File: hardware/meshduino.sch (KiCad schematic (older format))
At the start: 9 parts, among them P1 mPCIe, P2 USB, U1 SM200, U2 FT232RL

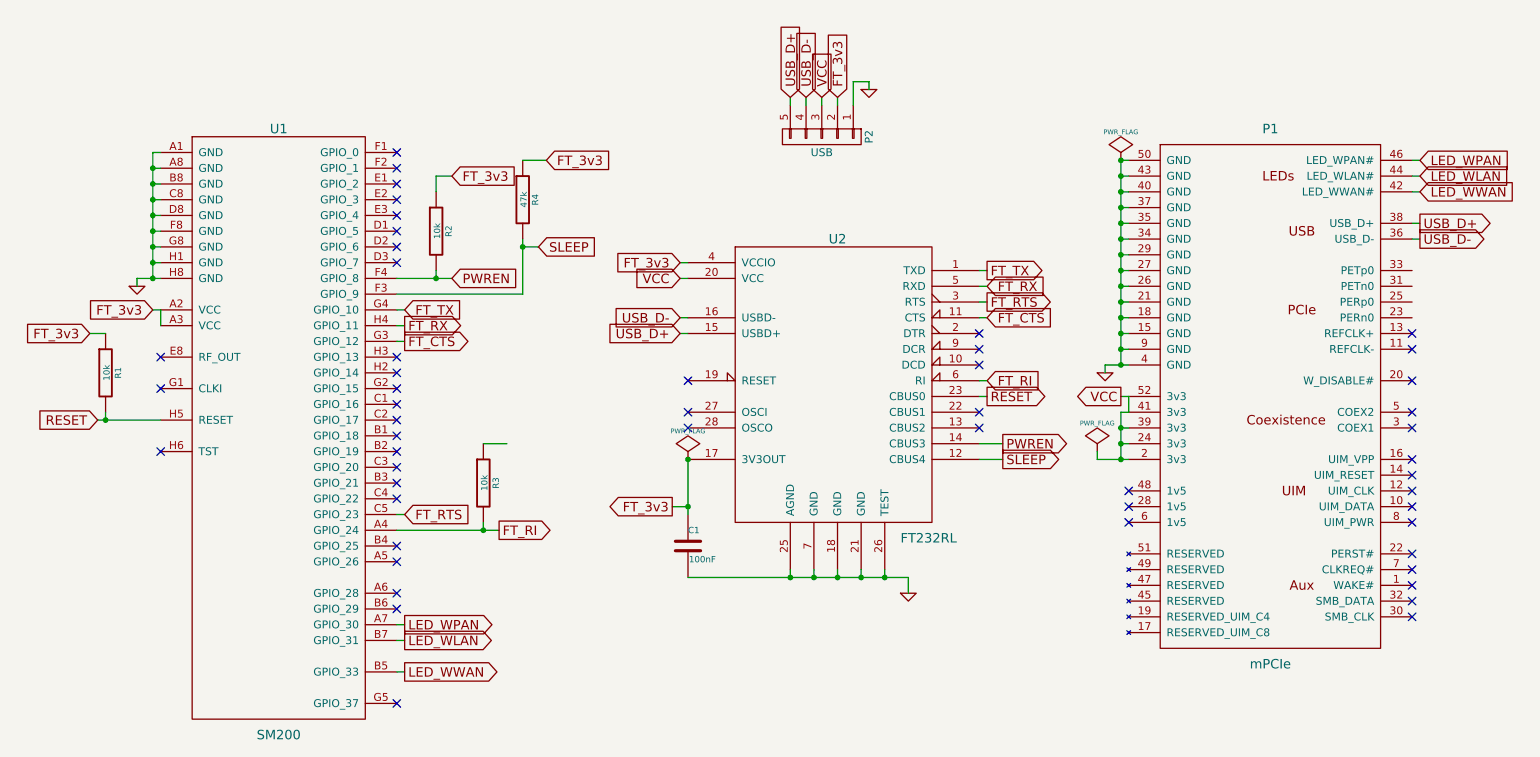
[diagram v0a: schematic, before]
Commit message: Replace pcie connector with USB connector.
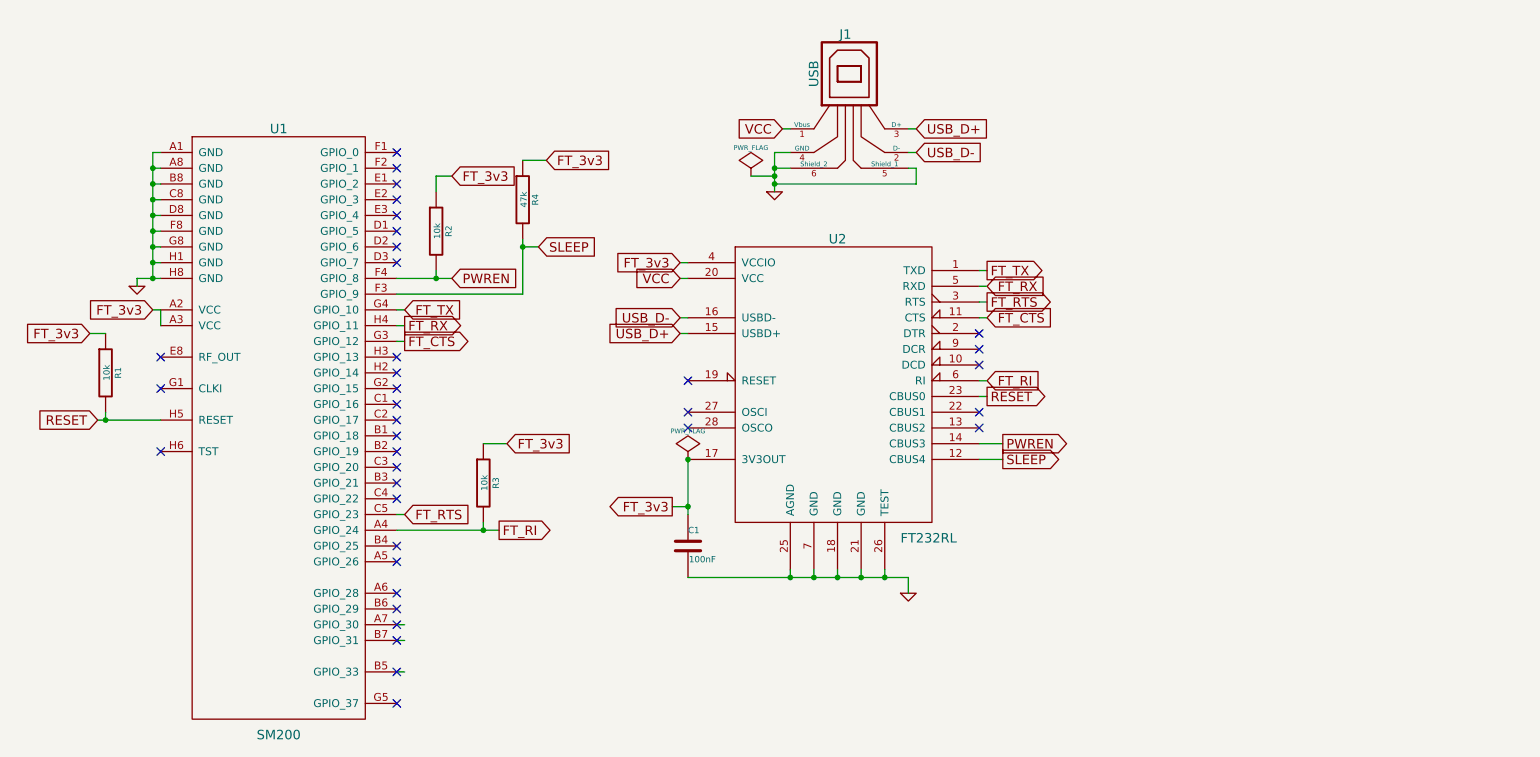
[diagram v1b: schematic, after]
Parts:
- removed P1: mPCIe, _CrumpPrints:MPCIe_full_card, symbol mPCIe
- removed P2: USB, Pin_Headers:Pin_Header_Straight_1x05, symbol CONN_01X05
- added J1: USB, symbol USB
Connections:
- net labels removed: LED_WLAN, LED_WPAN, LED_WWAN
- wire segments 91 -> 65
- no-connect marks 52 -> 37
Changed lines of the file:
@@
-$EndComp
-$Comp
-L mPCIe P1
-U 1 1 55C19570
-P 9350 3500
-F 0 "P1" H 9350 4900 60  0000 C CNN
-F 1 "mPCIe" H 9350 1500 60  0000 C CNN
-F 2 "_CrumpPrints:MPCIe_full_card" H 9350 3500 60  0001 C CNN
-F 3 "" H 9350 3500 60  0000 C CNN
-	1    9350 3500
-	1    0    0    -1
 $EndComp
 $Comp
@@
 	1    0    0    -1
 $EndComp
-Text GLabel 10300 2700 2    60   Output ~ 0
-USB_D+
-Text GLabel 10300 2800 2    60   Output ~ 0
-USB_D-
 Text GLabel 5600 3400 0    60   Input ~ 0
 USB_D+
@@
 USB_D-
 Text GLabel 5600 3050 0    60   Input ~ 0
-VCC
-Text GLabel 8400 3800 0    60   Output ~ 0
 VCC
 Text GLabel 2250 3250 0    60   Input ~ 0
@@
 Text GLabel 5600 2950 0    60   Input ~ 0
 FT_3v3
-Text GLabel 10300 2300 2    60   Input ~ 0
-LED_WPAN
-Text GLabel 10300 2400 2    60   Input ~ 0
-LED_WLAN
-Text GLabel 10300 2500 2    60   Input ~ 0
-LED_WWAN
-Text GLabel 3850 5550 2    60   Output ~ 0
-LED_WWAN
-Text GLabel 3850 5350 2    60   Output ~ 0
-LED_WLAN
-Text GLabel 3850 5250 2    60   Output ~ 0
-LED_WPAN
 $Comp
 L GND #PWR02
@@
 	1    0    0    -1
 $EndComp
-$Comp
-L GND #PWR03
-U 1 1 55FF26A9
-P 8300 3650
-F 0 "#PWR03" H 8300 3650 30  0001 C CNN
-F 1 "GND" H 8300 3580 30  0001 C CNN
-F 2 "" H 8300 3650 60  0000 C CNN
-F 3 "" H 8300 3650 60  0000 C CNN
-	1    8300 3650
-	1    0    0    -1
-$EndComp
 Wire Wire Line
 	5600 3300 5650 3300
 Wire Wire Line
 	5600 3400 5650 3400
-Wire Wire Line
-	10250 2700 10300 2700
-Wire Wire Line
-	10250 2800 10300 2800
-Wire Wire Line
-	8400 3800 8450 3800
 Wire Wire Line
 	5600 3050 5650 3050
@@
 	4600 3150 3800 3150
 Wire Wire Line
-	6450 4900 6450 4950
+	6450 4950 6450 4900
 Wire Wire Line
 	5650 4950 7050 4950
@@
 	4050 2400 4150 2400
 Wire Wire Line
-	10250 2500 10300 2500
-Wire Wire Line
-	10250 2400 10300 2400
-Wire Wire Line
-	10250 2300 10300 2300
-Wire Wire Line
 	3800 5250 3850 5250
 Wire Wire Line
@@
 	3800 5550 3850 5550
 Wire Wire Line
-	8450 2300 8400 2300
-Wire Wire Line
-	8400 2300 8400 3600
-Wire Wire Line
-	8400 2400 8450 2400
-Wire Wire Line
-	8400 2500 8450 2500
-Connection ~ 8400 2400
-Wire Wire Line
-	8400 2600 8450 2600
-Connection ~ 8400 2500
-Wire Wire Line
-	8400 2700 8450 2700
-Connection ~ 8400 2600
-Wire Wire Line
-	8400 2800 8450 2800
-Connection ~ 8400 2700
-Wire Wire Line
-	8400 2900 8450 2900
-Connection ~ 8400 2800
-Wire Wire Line
-	8400 3000 8450 3000
-Connection ~ 8400 2900
-Wire Wire Line
-	8400 3100 8450 3100
-Connection ~ 8400 3000
-Wire Wire Line
-	8400 3200 8450 3200
-Connection ~ 8400 3100
-Wire Wire Line
-	8400 3300 8450 3300
-Connection ~ 8400 3200
-Wire Wire Line
-	8400 3400 8450 3400
-Connection ~ 8400 3300
-Wire Wire Line
-	8400 3500 8450 3500
-Connection ~ 8400 3400
-Wire Wire Line
-	8300 3600 8450 3600
-Connection ~ 8400 3500
-Wire Wire Line
-	8450 3800 8450 3900
-Wire Wire Line
-	8400 3900 8400 4200
-Wire Wire Line
-	8400 4000 8450 4000
-Wire Wire Line
-	8450 3900 8400 3900
-Wire Wire Line
-	8400 4100 8450 4100
-Connection ~ 8400 4000
-Wire Wire Line
-	8250 4200 8450 4200
-Connection ~ 8400 4100
-Wire Wire Line
-	8300 3600 8300 3650
-Connection ~ 8400 3600
-Wire Wire Line
-	2300 3050 2150 3050
+	2150 3050 2300 3050
 Wire Wire Line
 	2150 3050 2150 3100
@@
 	2250 2250 2300 2250
 Connection ~ 2250 2350
-NoConn ~ 10250 3400
-NoConn ~ 10250 3500
-NoConn ~ 10250 3700
-NoConn ~ 10250 3900
-NoConn ~ 10250 4000
-NoConn ~ 10250 4200
-NoConn ~ 10250 4300
-NoConn ~ 10250 4400
-NoConn ~ 10250 4500
-NoConn ~ 10250 4600
-NoConn ~ 10250 4800
-NoConn ~ 10250 4900
-NoConn ~ 10250 5000
-NoConn ~ 10250 5100
-NoConn ~ 10250 5200
-NoConn ~ 8450 4600
-NoConn ~ 8450 4500
-NoConn ~ 8450 4400
 NoConn ~ 7500 3400
 NoConn ~ 7500 3500
@@
 NoConn ~ 3800 5150
 $Comp
-L PWR_FLAG #FLG04
-U 1 1 55FF3712
-P 8400 2300
-F 0 "#FLG04" H 8400 2395 30  0001 C CNN
-F 1 "PWR_FLAG" H 8400 2480 30  0000 C CNN
-F 2 "" H 8400 2300 60  0000 C CNN
-F 3 "" H 8400 2300 60  0000 C CNN
-	1    8400 2300
-	1    0    0    -1
-$EndComp
-Connection ~ 8400 2300
-$Comp
-L PWR_FLAG #FLG05
-U 1 1 55FF3839
-P 8250 4150
-F 0 "#FLG05" H 8250 4245 30  0001 C CNN
-F 1 "PWR_FLAG" H 8250 4330 30  0000 C CNN
-F 2 "" H 8250 4150 60  0000 C CNN
-F 3 "" H 8250 4150 60  0000 C CNN
-	1    8250 4150
-	1    0    0    -1
-$EndComp
-Wire Wire Line
-	8250 4150 8250 4200
-Connection ~ 8400 4200
-$Comp
-L PWR_FLAG #FLG06
+L PWR_FLAG #FLG03
 U 1 1 55FF4264
 P 5650 4200
-F 0 "#FLG06" H 5650 4295 30  0001 C CNN
+F 0 "#FLG03" H 5650 4295 30  0001 C CNN
 F 1 "PWR_FLAG" H 5650 4380 30  0000 C CNN
 F 2 "" H 5650 4200 60  0000 C CNN
@@
 Connection ~ 5650 4200
 $Comp
-L CONN_01X05 P2
-U 1 1 55FF44AF
-P 6500 2150
-F 0 "P2" H 6500 2450 50  0000 C CNN
-F 1 "USB" V 6600 2150 50  0000 C CNN
-F 2 "Pin_Headers:Pin_Header_Straight_1x05" H 6500 2150 60  0001 C CNN
-F 3 "" H 6500 2150 60  0000 C CNN
-	1    6500 2150
-	0    1    1    0
-$EndComp
-$Comp
-L GND #PWR07
+L GND #PWR04
 U 1 1 55FF454C
-P 6800 1850
-F 0 "#PWR07" H 6800 1850 30  0001 C CNN
-F 1 "GND" H 6800 1780 30  0001 C CNN
-F 2 "" H 6800 1850 60  0000 C CNN
-F 3 "" H 6800 1850 60  0000 C CNN
-	1    6800 1850
-	1    0    0    -1
-$EndComp
-Text GLabel 6500 1900 1    60   Input ~ 0
+P 6200 2500
+F 0 "#PWR04" H 6200 2500 30  0001 C CNN
+F 1 "GND" H 6200 2430 30  0001 C CNN
+F 2 "" H 6200 2500 60  0000 C CNN
+F 3 "" H 6200 2500 60  0000 C CNN
+	1    6200 2500
+	1    0    0    -1
+$EndComp
+Text GLabel 6250 2100 0    60   Input ~ 0
 VCC
-Text GLabel 6600 1900 1    60   Input ~ 0
-FT_3v3
-Text GLabel 6400 1900 1    60   Input ~ 0
+Text GLabel 7100 2250 2    60   Input ~ 0
 USB_D-
-Text GLabel 6300 1900 1    60   Input ~ 0
+Text GLabel 7100 2100 2    60   Input ~ 0
 USB_D+
-Wire Wire Line
-	6800 1850 6800 1800
-Wire Wire Line
-	6800 1800 6700 1800
-Wire Wire Line
-	6700 1800 6700 1950
-Wire Wire Line
-	6600 1900 6600 1950
-Wire Wire Line
-	6500 1950 6500 1900
-Wire Wire Line
-	6400 1900 6400 1950
-Wire Wire Line
-	6300 1950 6300 1900
 NoConn ~ 5650 3900
 NoConn ~ 5650 4000
+$Comp
+L USB J1
+U 1 1 56207A99
+P 6700 1900
+F 0 "J1" H 6650 2300 60  0000 C CNN
+F 1 "USB" V 6450 2050 60  0000 C CNN
+F 2 "" H 6700 1900 60  0000 C CNN
+F 3 "" H 6700 1900 60  0000 C CNN
+	1    6700 1900
+	1    0    0    -1
+$EndComp
+Wire Wire Line
+	6250 2100 6300 2100
+Wire Wire Line
+	6300 2250 6200 2250
+Wire Wire Line
+	6200 2250 6200 2500
+Wire Wire Line
+	6300 2350 6200 2350
+Connection ~ 6200 2350
+Wire Wire Line
+	7050 2100 7100 2100
+Wire Wire Line
+	7050 2250 7100 2250
+Wire Wire Line
+	7050 2350 7100 2350
+Wire Wire Line
+	7100 2350 7100 2450
+Wire Wire Line
+	7100 2450 6200 2450
+Connection ~ 6200 2450
+NoConn ~ 3800 5250
+NoConn ~ 3800 5350
+NoConn ~ 3800 5550
+$Comp
+L PWR_FLAG #FLG05
+U 1 1 56208562
+P 6050 2400
+F 0 "#FLG05" H 6050 2495 30  0001 C CNN
+F 1 "PWR_FLAG" H 6050 2580 30  0000 C CNN
+F 2 "" H 6050 2400 60  0000 C CNN
+F 3 "" H 6050 2400 60  0000 C CNN
+	1    6050 2400
+	1    0    0    -1
+$EndComp
+Wire Wire Line
+	6050 2400 6200 2400
+Connection ~ 6200 2400
+Text GLabel 4500 4100 2    60   Input ~ 0
+FT_3v3
 $EndSCHEMATC

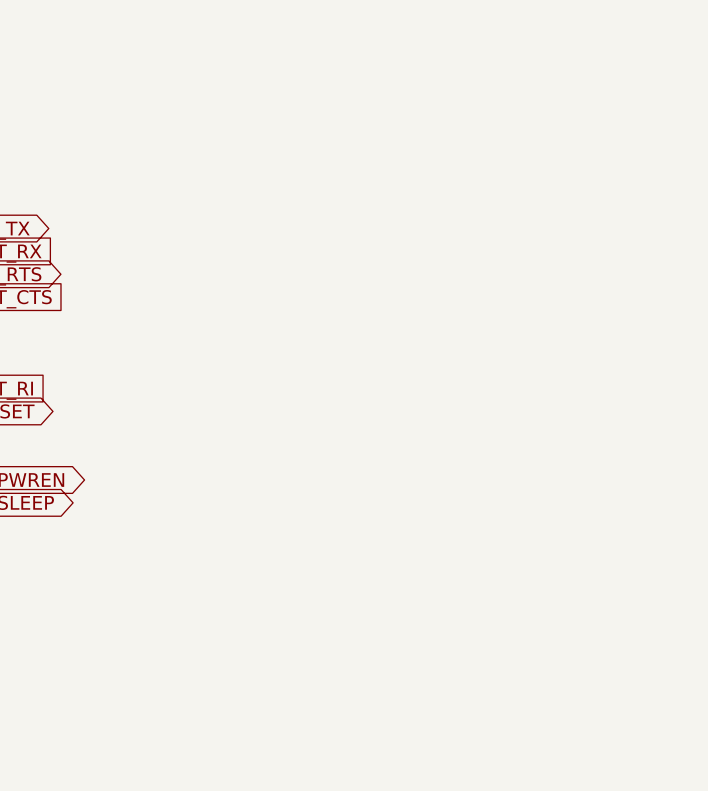
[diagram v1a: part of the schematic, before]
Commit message: Add pin headers to schematic.
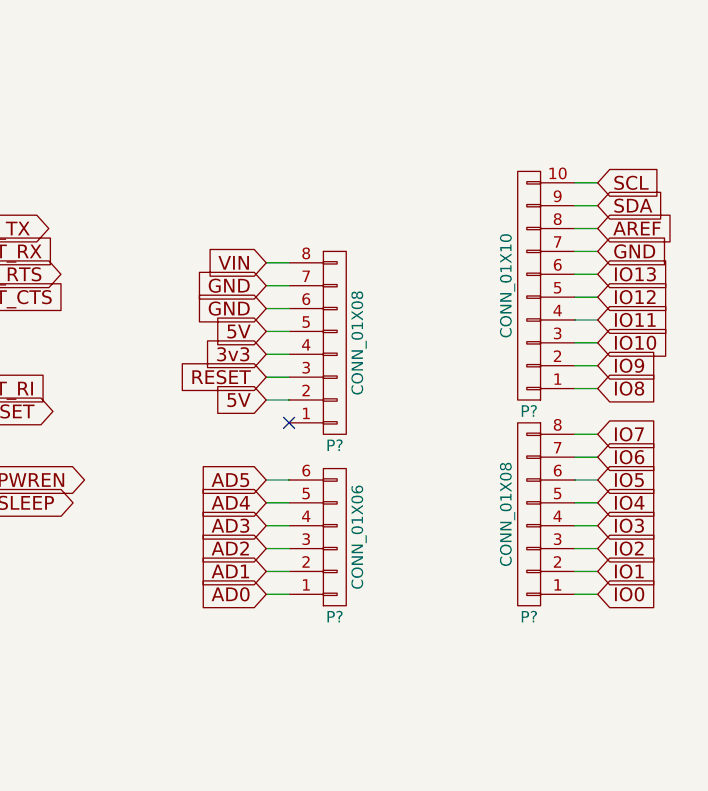
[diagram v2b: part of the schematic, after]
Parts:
- added P?: CONN_01X06, symbol CONN_01X06
- added P? (x2): CONN_01X08, symbol CONN_01X08
- added P?: CONN_01X10, symbol CONN_01X10
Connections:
- net labels added: 3v3, 5V, AD0, AD1, AD2, AD3, AD4, AD5, AREF, IO0, IO1, IO10, IO11, IO12, IO13, IO2, IO3, IO4, IO5, IO6, IO7, IO8, IO9, SCL, SDA, VIN
- wire segments 65 -> 96
- no-connect marks 37 -> 38
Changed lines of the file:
@@
 Text GLabel 4500 4100 2    60   Input ~ 0
 FT_3v3
+$Comp
+L CONN_01X06 P?
+U 1 1 56208AD2
+P 9150 4350
+F 0 "P?" H 9150 4700 50  0000 C CNN
+F 1 "CONN_01X06" V 9250 4350 50  0000 C CNN
+F 2 "" H 9150 4350 60  0000 C CNN
+F 3 "" H 9150 4350 60  0000 C CNN
+	1    9150 4350
+	1    0    0    1
+$EndComp
+$Comp
+L CONN_01X08 P?
+U 1 1 56208B19
+P 9150 3500
+F 0 "P?" H 9150 3950 50  0000 C CNN
+F 1 "CONN_01X08" V 9250 3500 50  0000 C CNN
+F 2 "" H 9150 3500 60  0000 C CNN
+F 3 "" H 9150 3500 60  0000 C CNN
+	1    9150 3500
+	1    0    0    1
+$EndComp
+$Comp
+L CONN_01X08 P?
+U 1 1 56208BBE
+P 10000 4250
+F 0 "P?" H 10000 4700 50  0000 C CNN
+F 1 "CONN_01X08" V 10100 4250 50  0000 C CNN
+F 2 "" H 10000 4250 60  0000 C CNN
+F 3 "" H 10000 4250 60  0000 C CNN
+	1    10000 4250
+	-1   0    0    1
+$EndComp
+$Comp
+L CONN_01X10 P?
+U 1 1 56208C0F
+P 10000 3250
+F 0 "P?" H 10000 3800 50  0000 C CNN
+F 1 "CONN_01X10" V 10100 3250 50  0000 C CNN
+F 2 "" H 10000 3250 60  0000 C CNN
+F 3 "" H 10000 3250 60  0000 C CNN
+	1    10000 3250
+	-1   0    0    1
+$EndComp
+Text GLabel 10300 4600 2    60   Input ~ 0
+IO0
+Text GLabel 10300 4500 2    60   Input ~ 0
+IO1
+Text GLabel 10300 4400 2    60   Input ~ 0
+IO2
+Text GLabel 10300 4300 2    60   Input ~ 0
+IO3
+Text GLabel 10300 4200 2    60   Input ~ 0
+IO4
+Text GLabel 10300 4100 2    60   Input ~ 0
+IO5
+Text GLabel 10300 4000 2    60   Input ~ 0
+IO6
+Text GLabel 10300 3900 2    60   Input ~ 0
+IO7
+Text GLabel 10300 3700 2    60   Input ~ 0
+IO8
+Text GLabel 10300 3600 2    60   Input ~ 0
+IO9
+Text GLabel 10300 3500 2    60   Input ~ 0
+IO10
+Text GLabel 10300 3400 2    60   Input ~ 0
+IO11
+Text GLabel 10300 3300 2    60   Input ~ 0
+IO12
+Text GLabel 10300 3200 2    60   Input ~ 0
+IO13
+Text GLabel 10300 3100 2    60   Input ~ 0
+GND
+Text GLabel 10300 3000 2    60   Input ~ 0
+AREF
+Text GLabel 10300 2900 2    60   Input ~ 0
+SDA
+Text GLabel 10300 2800 2    60   Input ~ 0
+SCL
+Text GLabel 8850 4600 0    60   Input ~ 0
+AD0
+Text GLabel 8850 4500 0    60   Input ~ 0
+AD1
+Text GLabel 8850 4400 0    60   Input ~ 0
+AD2
+Text GLabel 8850 4300 0    60   Input ~ 0
+AD3
+Text GLabel 8850 4200 0    60   Input ~ 0
+AD4
+Text GLabel 8850 4100 0    60   Input ~ 0
+AD5
+Text GLabel 8850 3150 0    60   Input ~ 0
+VIN
+Text GLabel 8850 3250 0    60   Input ~ 0
+GND
+Text GLabel 8850 3350 0    60   Input ~ 0
+GND
+Text GLabel 8850 3450 0    60   Input ~ 0
+5V
+Text GLabel 8850 3550 0    60   Input ~ 0
+3v3
+Text GLabel 8850 3650 0    60   Input ~ 0
+RESET
+Text GLabel 8850 3750 0    60   Input ~ 0
+5V
+NoConn ~ 8950 3850
+Wire Wire Line
+	8850 3150 8950 3150
+Wire Wire Line
+	8950 3250 8850 3250
+Wire Wire Line
+	8850 3350 8950 3350
+Wire Wire Line
+	8950 3450 8850 3450
+Wire Wire Line
+	8850 3550 8950 3550
+Wire Wire Line
+	8950 3650 8850 3650
+Wire Wire Line
+	8850 3750 8950 3750
+Wire Wire Line
+	8950 4100 8850 4100
+Wire Wire Line
+	8850 4200 8950 4200
+Wire Wire Line
+	8950 4300 8850 4300
+Wire Wire Line
+	8850 4400 8950 4400
+Wire Wire Line
+	8950 4500 8850 4500
+Wire Wire Line
+	8850 4600 8950 4600
+Wire Wire Line
+	10200 4600 10300 4600
+Wire Wire Line
+	10300 4500 10200 4500
+Wire Wire Line
+	10200 4400 10300 4400
+Wire Wire Line
+	10300 4300 10200 4300
+Wire Wire Line
+	10200 4200 10300 4200
+Wire Wire Line
+	10300 4100 10200 4100
+Wire Wire Line
+	10200 4000 10300 4000
+Wire Wire Line
+	10300 3900 10200 3900
+Wire Wire Line
+	10200 3700 10300 3700
+Wire Wire Line
+	10300 3600 10200 3600
+Wire Wire Line
+	10200 3500 10300 3500
+Wire Wire Line
+	10300 3400 10200 3400
+Wire Wire Line
+	10200 3300 10300 3300
+Wire Wire Line
+	10300 3200 10200 3200
+Wire Wire Line
+	10200 3100 10300 3100
+Wire Wire Line
+	10300 3000 10200 3000
+Wire Wire Line
+	10200 2900 10300 2900
+Wire Wire Line
+	10300 2800 10200 2800
 $EndSCHEMATC
